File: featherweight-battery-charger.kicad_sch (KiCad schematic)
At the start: 16 parts, among them J1 G125-MH104M4-04AD000P, J2 Conn_01x02, U1 MCP73832-2-OT, U2 TPS561208DDCR

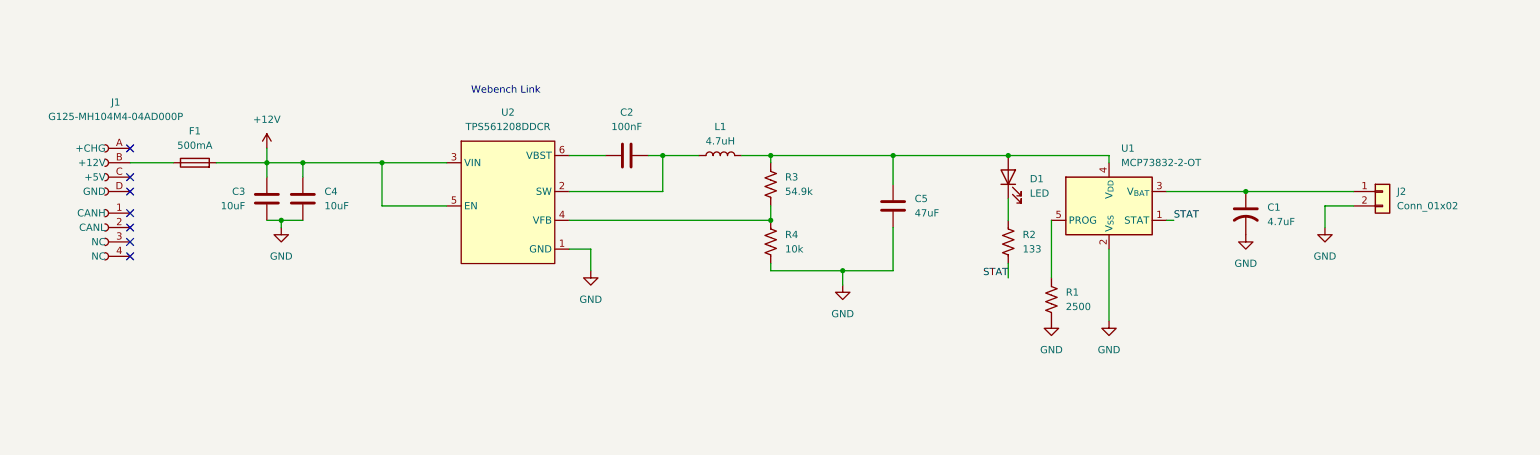
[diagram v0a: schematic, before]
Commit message: Added New Buck and Kicad Footprints Submodule
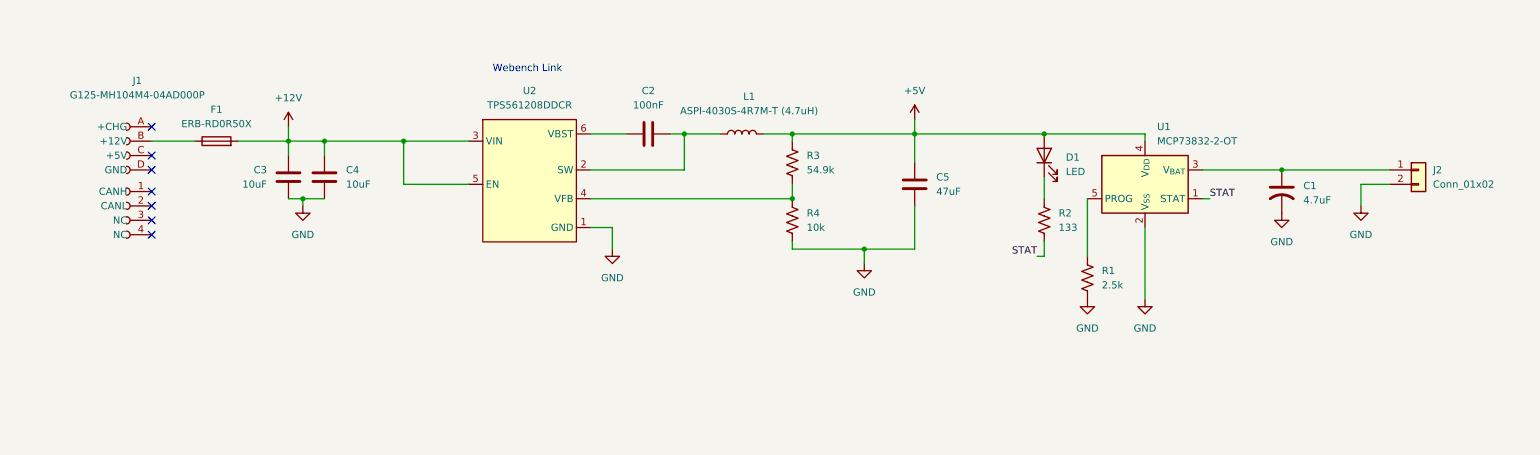
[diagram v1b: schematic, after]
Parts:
- C1, C2, C3, C4, C5: footprint (none) -> Capacitor_SMD:C_0201_0603Metric_Pad0.64x0.40mm_HandSolder
- D1: footprint (none) -> LED_SMD:LED_1206_3216Metric_Pad1.42x1.75mm_HandSolder
- F1: value 500mA -> ERB-RD0R50X; footprint (none) -> Fuse:Fuse_0402_1005Metric_Pad0.77x0.64mm_HandSolder
- J1: footprint canhw_footprints:HARWIN_G125-MH104M4-04AD000P -> canhw:connector_Harwin_G125-MH104M4-04AD000P
- J2: footprint (none) -> Connector_JST:JST_XH_B2B-XH-AM_1x02_P2.50mm_Vertical
- L1: value 4.7uH -> ASPI-4030S-4R7M-T (4.7uH); footprint (none) -> Inductor_SMD:L_Abracon_ASPI-4030S
- R1: value 2500 -> 2.5k; footprint (none) -> Resistor_SMD:R_0201_0603Metric_Pad0.64x0.40mm_HandSolder
- R2, R3, R4: footprint (none) -> Resistor_SMD:R_0201_0603Metric_Pad0.64x0.40mm_HandSolder
- U2: footprint (none) -> Package_TO_SOT_SMD:TSOT-23-6_HandSoldering
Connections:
- net +5V: now reaches C5.2, D1.2 (A), L1.2, R3.2, U1.4 (V_{DD})
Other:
- moved on the sheet: C1, C2, C3, C4, C5, D1, F1, J1, L1, R1, R2, R3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

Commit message: Started Layout and Routing
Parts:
- L1: value ASPI-4030S-4R7M-T (4.7uH) -> NRS4018T4R7MDGJ (4.7uH); footprint Inductor_SMD:L_Abracon_ASPI-4030S -> Inductor_SMD:L_Taiyo-Yuden_NR-40xx_HandSoldering
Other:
- moved on the sheet: C2, C4

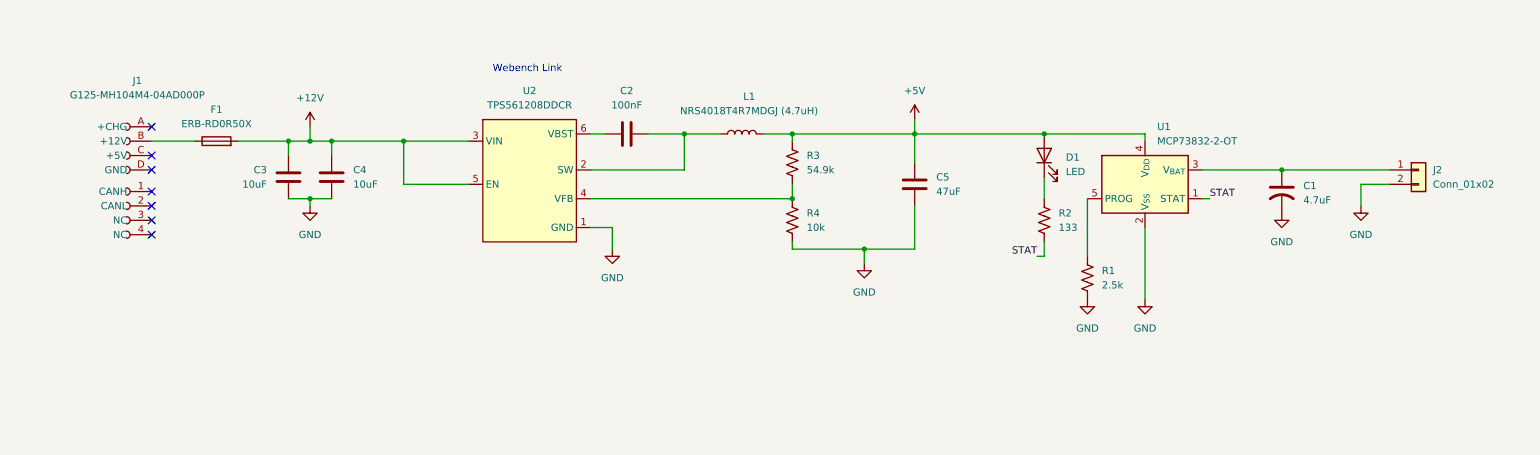
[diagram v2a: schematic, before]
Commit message: Did most of the layout and routing, need to finish silkscreen and then check everything
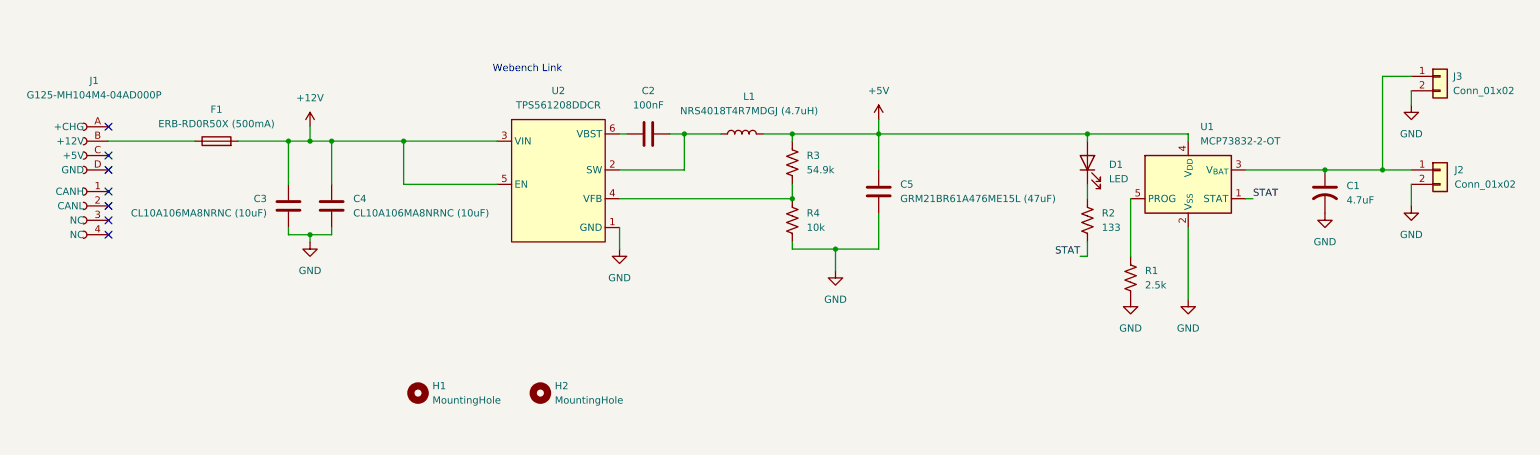
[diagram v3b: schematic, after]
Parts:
- added H1, H2: MountingHole, MountingHole:MountingHole_3.2mm_M3, symbol Mechanical:MountingHole
- added J3: Conn_01x02, Connector_JST:JST_XH_B2B-XH-AM_1x02_P2.50mm_Vertical, symbol Connector_Generic:Conn_01x02
- C1, C2: footprint Capacitor_SMD:C_0201_0603Metric_Pad0.64x0.40mm_HandSolder -> Capacitor_SMD:C_0603_1608Metric_Pad1.08x0.95mm_HandSolder
- C3, C4: value 10uF -> CL10A106MA8NRNC (10uF); footprint Capacitor_SMD:C_0201_0603Metric_Pad0.64x0.40mm_HandSolder -> Capacitor_SMD:C_0603_1608Metric_Pad1.08x0.95mm_HandSolder
- C5: value 47uF -> GRM21BR61A476ME15L (47uF); footprint Capacitor_SMD:C_0201_0603Metric_Pad0.64x0.40mm_HandSolder -> Capacitor_SMD:C_0805_2012Metric_Pad1.18x1.45mm_HandSolder
- F1: value ERB-RD0R50X -> ERB-RD0R50X (500mA)
- R1, R2, R3, R4: footprint Resistor_SMD:R_0201_0603Metric_Pad0.64x0.40mm_HandSolder -> Resistor_SMD:R_0603_1608Metric_Pad0.98x0.95mm_HandSolder
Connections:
- net GND: now also J3.2 (Pin_2)
- net at C1.1, J2.1 (Pin_1), U1.3 (V_{BAT}): now also J3.1 (Pin_1)
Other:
- moved on the sheet: C1, C2, C3, C4, C5, D1, J1, J2, R1, R2, U1, U2

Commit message: Forgot the schematic changes
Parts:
- added C6, C7: 0.1uF, Capacitor_SMD:C_0603_1608Metric_Pad1.08x0.95mm_HandSolder, symbol Device:C
- J2, J3: footprint Connector_JST:JST_XH_B2B-XH-AM_1x02_P2.50mm_Vertical -> Connector_JST:JST_PH_S2B-PH-K_1x02_P2.00mm_Horizontal
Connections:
- net +12V: now also C6.1
- net +5V: now also C7.1
- net GND: now also C6.2, C7.2
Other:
- moved on the sheet: R1

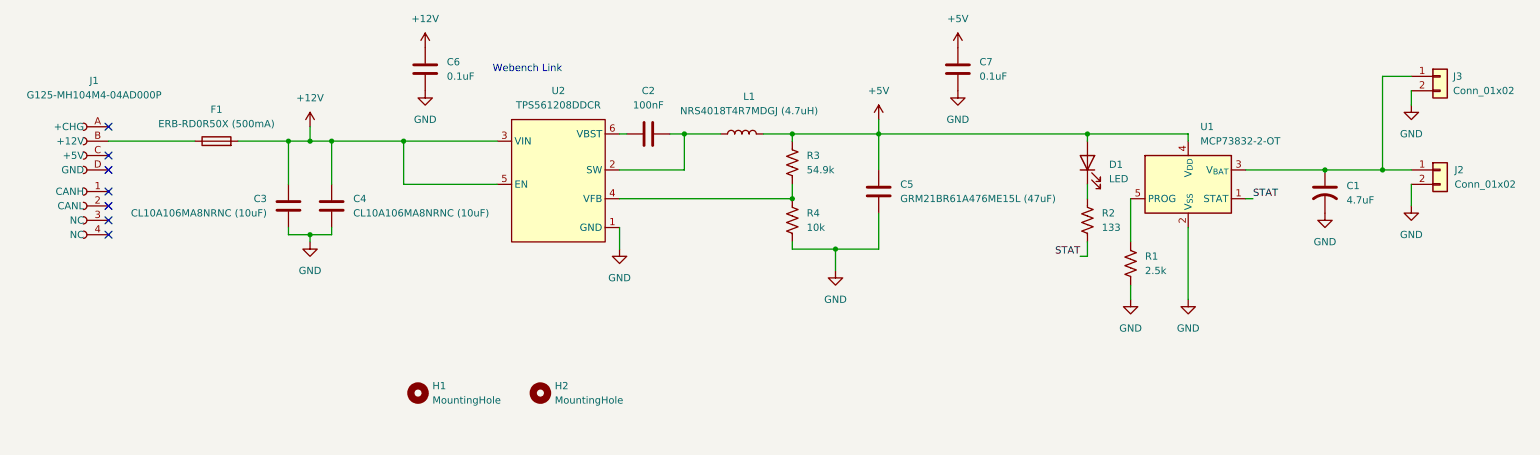
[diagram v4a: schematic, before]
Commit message: Changed Layout and Routing
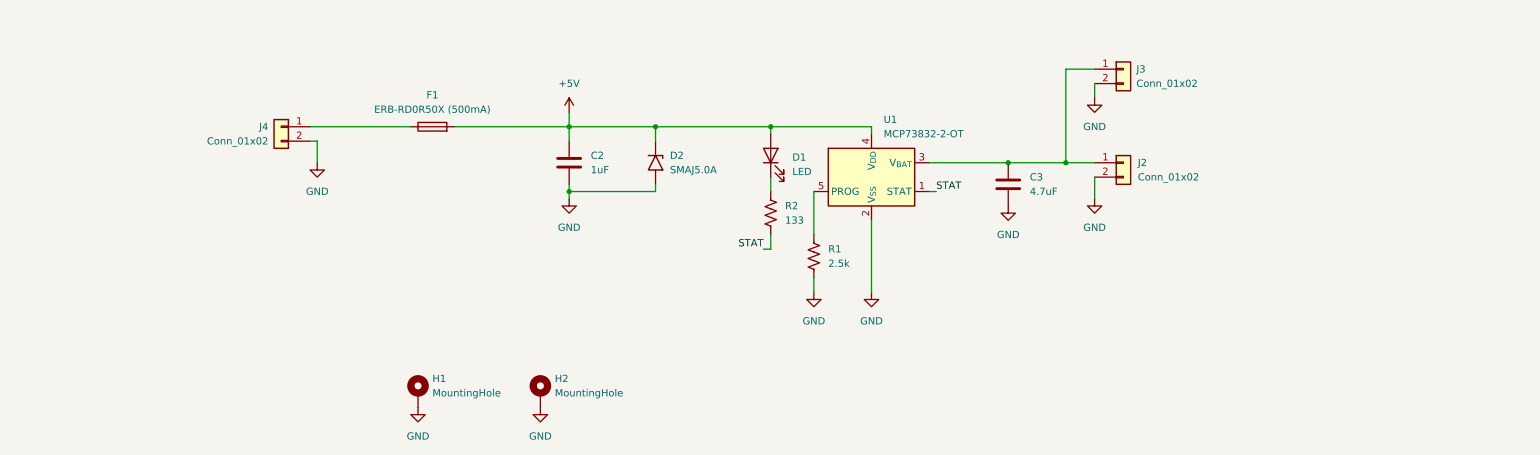
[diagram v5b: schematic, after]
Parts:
- removed C1: 4.7uF, Capacitor_SMD:C_0603_1608Metric_Pad1.08x0.95mm_HandSolder, symbol Device:C_US
- removed C4: CL10A106MA8NRNC (10uF), Capacitor_SMD:C_0603_1608Metric_Pad1.08x0.95mm_HandSolder, symbol Device:C
- removed C5: GRM21BR61A476ME15L (47uF), Capacitor_SMD:C_0805_2012Metric_Pad1.18x1.45mm_HandSolder, symbol Device:C
- removed C6, C7: 0.1uF, Capacitor_SMD:C_0603_1608Metric_Pad1.08x0.95mm_HandSolder, symbol Device:C
- removed J1: G125-MH104M4-04AD000P, canhw:connector_Harwin_G125-MH104M4-04AD000P, symbol canhw:G125-MH104M4-04AD000P
- removed L1: NRS4018T4R7MDGJ (4.7uH), Inductor_SMD:L_Taiyo-Yuden_NR-40xx_HandSoldering, symbol Device:L
- removed R3: 54.9k, Resistor_SMD:R_0603_1608Metric_Pad0.98x0.95mm_HandSolder, symbol Device:R_US
- removed R4: 10k, Resistor_SMD:R_0603_1608Metric_Pad0.98x0.95mm_HandSolder, symbol Device:R_US
- removed U2: TPS561208DDCR, Package_TO_SOT_SMD:TSOT-23-6_HandSoldering, symbol TPS561208DDCR:TPS561208DDC
- added D2: SMAJ5.0A, Diode_SMD:D_SMA, symbol Diode:SMAJ5.0A
- added J4: Conn_01x02, Connector_JST:JST_VH_S2P-VH_1x02_P3.96mm_Horizontal, symbol Connector_Generic:Conn_01x02
- C2: value 100nF -> 1uF
- C3: value CL10A106MA8NRNC (10uF) -> 4.7uF
- H1, H2: footprint MountingHole:MountingHole_3.2mm_M3 -> MountingHole:MountingHole_3.2mm_M3_Pad; symbol Mechanical:MountingHole -> Mechanical:MountingHole_Pad
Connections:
- net +5V: now also C2.1, F1.2, D2.1 (A1)
- net GND: now also C2.2, H1.1, H2.1, D2.2 (A2), J4.2 (Pin_2)
- net at F1.1: now also J4.1 (Pin_1)
- net at J2.1 (Pin_1), J3.1 (Pin_1), U1.3 (V_{BAT}): now also C3.1
- removed net +12V: C3.1, F1.2
- no-connect marks 7 -> 0
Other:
- note removed: "Webench Link"
- moved on the sheet: D1, F1, J2, J3, R1, R2, U1

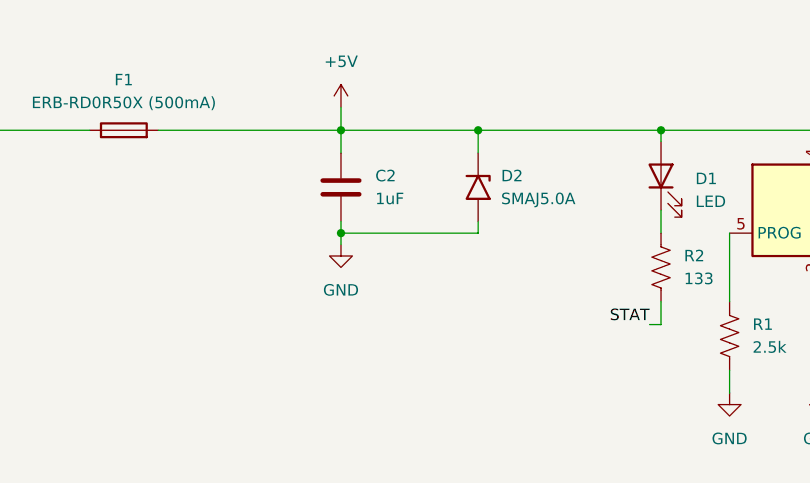
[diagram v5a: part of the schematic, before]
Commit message: Change C2 from 1uF to 4.7uF
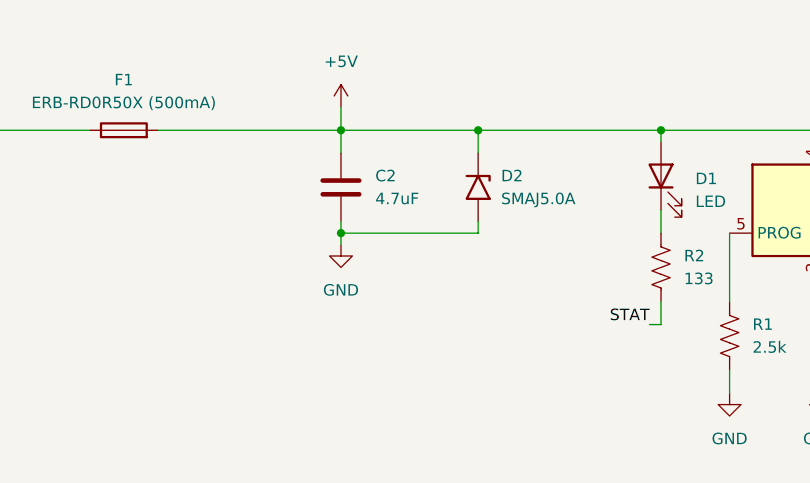
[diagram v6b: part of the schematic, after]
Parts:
- C2: value 1uF -> 4.7uF
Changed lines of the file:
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@@
 			)
 		)
-		(property "Value" "1uF"
+		(property "Value" "4.7uF"
 			(at 116.84 102.8699 0)
 			(effects

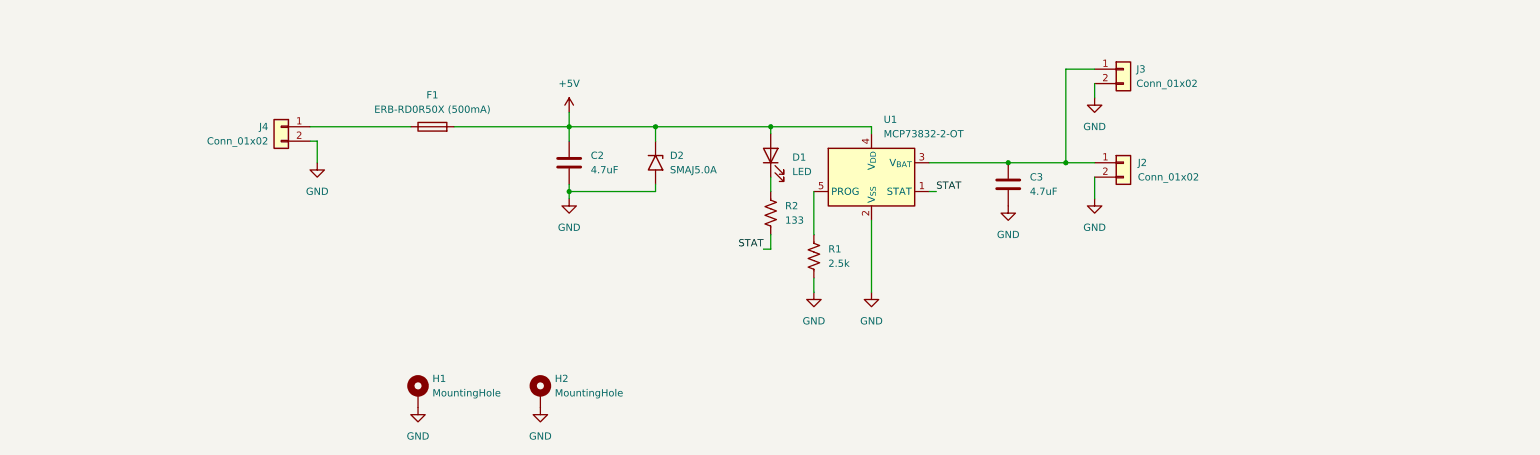
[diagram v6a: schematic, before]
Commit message: Changed Layout and Routing, Added Calculation Comments and Batt plane for  heat diff. Fuse changed to 1206
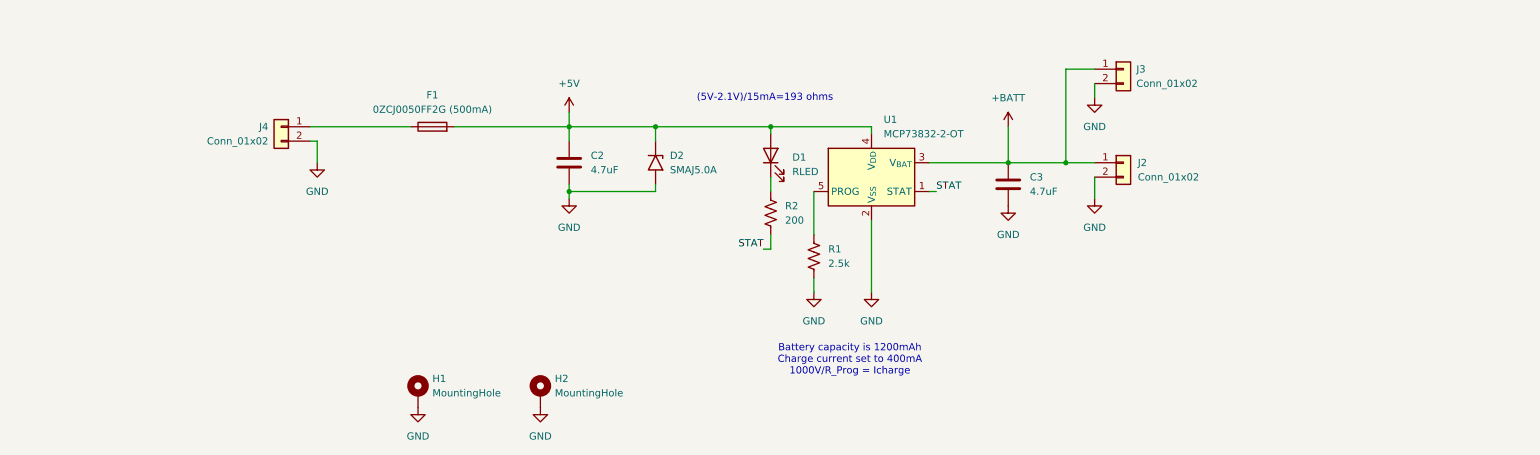
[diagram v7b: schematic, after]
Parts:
- D1: value LED -> RLED
- F1: value ERB-RD0R50X (500mA) -> 0ZCJ0050FF2G (500mA); footprint Fuse:Fuse_0402_1005Metric_Pad0.77x0.64mm_HandSolder -> Fuse:Fuse_1206_3216Metric_Pad1.42x1.75mm_HandSolder
- R2: value 133 -> 200
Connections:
- net +BATT: now reaches C3.1, J2.1 (Pin_1), J3.1 (Pin_1), U1.3 (V_{BAT})
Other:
- note added: "(5V-2.1V)/15mA=193 ohms"
- note added: "Battery capacity is 1200mAh Charge current set to 400mA 1000V/R_Prog = Icharge"
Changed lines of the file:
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@@
 	(generator_version "9.0")
 	(paper "A4")
+	(text "Battery capacity is 1200mAh\nCharge current set to 400mA\n1000V/R_Prog = Icharge"
+		(exclude_from_sim no)
+		(at 162.56 136.398 0)
+		(effects
+			(font
+				(size 1.27 1.27)
+			)
+		)
+	)
+	(text "(5V-2.1V)/15mA=193 ohms"
+		(exclude_from_sim no)
+		(at 147.574 90.17 0)
+		(effects
+			(font
+				(size 1.27 1.27)
+			)
+		)
+	)
 	(junction
 		(at 113.03 95.25)
@@
 		(pts
 			(xy 92.71 95.25) (xy 113.03 95.25)
+		)
+		(stroke
+			(width 0)
+			(type default)
+		)
+	)
+	(wire
+		(pts
+			(xy 190.5 95.25) (xy 190.5 101.6)
 		)
 		(stroke
@@
 			)
 		)
-		(property "Value" "ERB-RD0R50X (500mA)"
+		(property "Value" "0ZCJ0050FF2G (500mA)"
 			(at 88.9 92.202 90)
 			(effects
@@
 			)
 		)
-		(property "Footprint" "Fuse:Fuse_0402_1005Metric_Pad0.77x0.64mm_HandSolder"
+		(property "Footprint" "Fuse:Fuse_1206_3216Metric_Pad1.42x1.75mm_HandSolder"
 			(at 88.9 97.028 90)
 			(effects
@@
 			)
 		)
-		(property "Datasheet" "https://industrial.panasonic.com/cdbs/www-data/pdf/AFA0000/AFA0000C7.pdf"
+		(property "Datasheet" "https://www.belfuse.com/media/datasheets/products/circuit-protection/ds-cp-0zcj-series.pdf"
 			(at 88.9 95.25 0)
 			(effects
@@
 			)
 		)
-		(property "Value" "LED"
+		(property "Value" "RLED"
 			(at 152.4 103.1874 90)
 			(effects
@@
 			)
 		)
-		(property "Value" "133"
+		(property "Value" "200"
 			(at 151.13 111.7599 0)
 			(effects
@@
 					(unit 1)
 				)
+			)
+		)
+	)
+	(symbol
+		(lib_id "power:+BATT")
+		(at 190.5 95.25 0)
+		(unit 1)
+		(exclude_from_sim no)
+		(in_bom yes)
+		(on_board yes)
+		(dnp no)
+		(fields_autoplaced yes)
+		(property "Reference" "#PWR011"
+			(at 190.5 99.06 0)
+			(effects
+				(font
+					(size 1.27 1.27)
+				)
+				(hide yes)
+			)
+		)
+		(property "Value" "+BATT"
+			(at 190.5 90.17 0)
+			(effects
+				(font
+					(size 1.27 1.27)
+				)
+			)
+		)
+		(property "Footprint" ""
+			(at 190.5 95.25 0)
+			(effects
+				(font
+					(size 1.27 1.27)
+				)
+				(hide yes)
+			)
+		)
+		(property "Datasheet" ""
+			(at 190.5 95.25 0)
+			(effects
+				(font
+					(size 1.27 1.27)
+				)
+				(hide yes)
+			)
+		)
+		(property "Description" "Power symbol creates a global label with name \"+BATT\""
+			(at 190.5 95.25 0)
+			(effects
+				(font
+					(size 1.27 1.27)
+				)
+				(hide yes)
+			)
+		)
+		(pin "1"
+		)
+		(instances
+			(project ""
+				(path "/5889f758-61b0-4051-8dd5-ccc851807563"
+					(reference "#PWR011")
+					(unit 1)
+				)
